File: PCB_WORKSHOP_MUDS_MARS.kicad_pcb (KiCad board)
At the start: 2 copper layers, 44.7 x 72.4 mm, 48 parts, among them J1 Conn_01x02_Pin, J2 Conn_01x02_Pin, J3 Conn_01x15_Socket, J4 Conn_01x15_Socket, J5 Conn_01x15_Socket, J6 Conn_01x02_Pin, M1 SI2300, SW1 SW_Push, U1 L9110S

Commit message: Silk screen adjustments
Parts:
- added G***: LOGO, LOGO, F.Cu at (168.1, 124.5)
- moved G*** 6.60 mm to (177.3, 124.7)
- renumbered J2 to J1, J6 to J2, J1 to J3, J3 to J4, J4 to J5, J5 to J6, M1 to U2
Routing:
- net KITC_GND: track 105.5 -> 134.0 mm
- net M_VCC: track 74.6 -> 70.0 mm
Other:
- board text added: "&"
- board text added: "A"
- board text added: "B"
- board text added: "BTN"
- board text added: "GND"
- board text added: "L1"
- board text added: "L10"
- board text added: "L11"
- board text added: "L2"
- board text added: "L3"
- board text added: "L4"
- board text added: "L5"
- board text added: "L6"
- board text added: "L7"
- board text added: "L8"
- board text added: "L9"
- board text added: "M1"
- board text added: "M1A"
- board text added: "M1B"
- board text added: "M2"

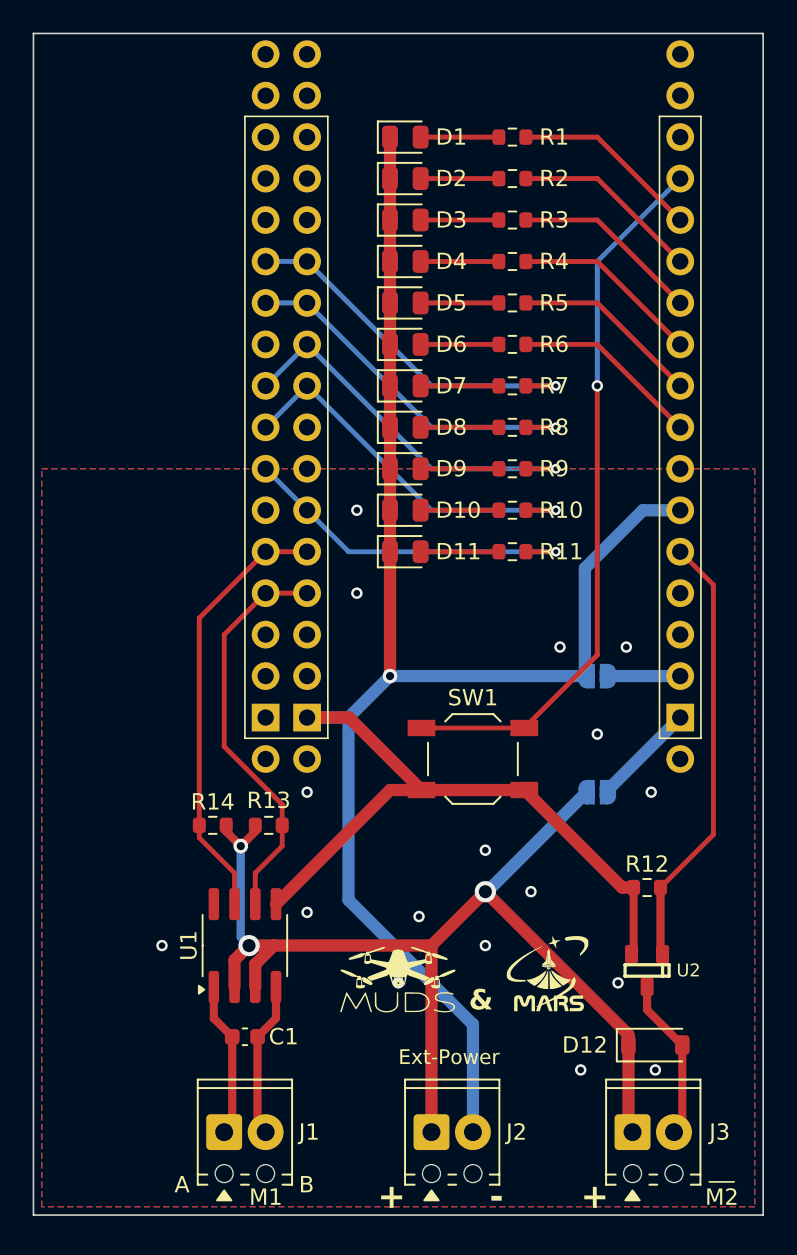
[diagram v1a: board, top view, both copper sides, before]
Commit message: added README, fixed examples
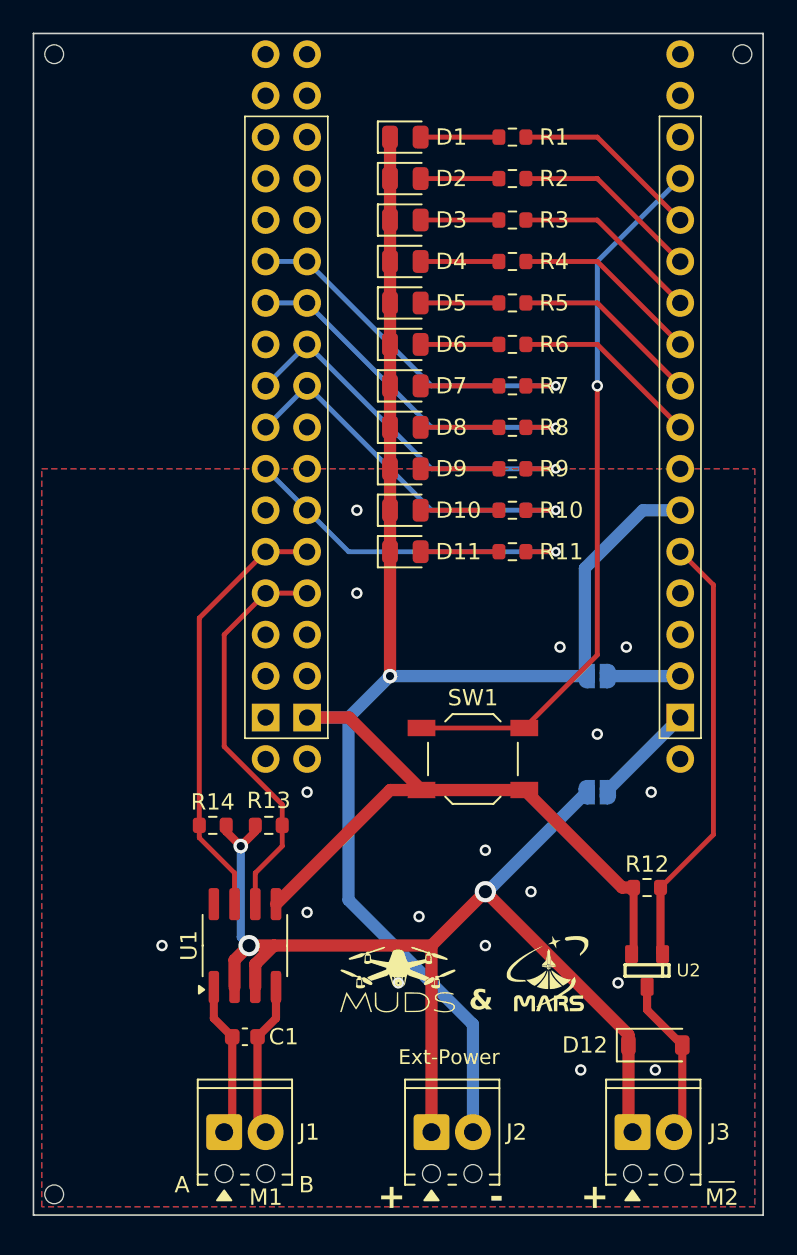
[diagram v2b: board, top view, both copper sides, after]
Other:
- outline, holes or cut-outs redrawn
- board text added: "JLCJLCJLCJLC"
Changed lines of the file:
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@@
+		(layer "Edge.Cuts")
+	)
+	(gr_circle
+		(center 189.23 68.58)
+		(end 189.806 68.58)
+		(stroke
+			(width 0.05)
+			(type solid)
+		)
+		(fill no)
+		(layer "Edge.Cuts")
+	)
+	(gr_circle
+		(center 147.066 68.58)
+		(end 147.642 68.58)
+		(stroke
+			(width 0.05)
+			(type solid)
+		)
+		(fill no)
+		(layer "Edge.Cuts")
+	)
+	(gr_circle
+		(center 147.066 138.43)
+		(end 147.642 138.43)
+		(stroke
+			(width 0.05)
+			(type solid)
+		)
+		(fill no)
 		(layer "Edge.Cuts")
 	)
@@
 		)
 	)
+	(gr_text "JLCJLCJLCJLC"
+		(at 173.736 102.87 90)
+		(layer "B.SilkS")
+		(effects
+			(font
+				(size 1 1)
+				(thickness 0.1)
+			)
+			(justify left bottom mirror)
+		)
+	)

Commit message: Forgot silkscreen blocks
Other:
- board text added: "BOPPIT Game"
- board text added: "H-Bridge Driver"
- board text added: "UniDir Motor Driver"
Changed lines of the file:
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@@
 		(tags "resistor")
 		(property "Reference" "R14"
-			(at 0 -1.43 0)
+			(at 0 1.524 0)
 			(layer "F.SilkS")
 			(effects
@@
 		(tags "capacitor")
 		(property "Reference" "C1"
-			(at 2.375 0 0)
+			(at -2.54 0 0)
 			(layer "F.SilkS")
 			(effects
@@
 		(tags "resistor")
 		(property "Reference" "R13"
-			(at 0 1.524 0)
+			(at 0 -1.524 0)
 			(layer "F.SilkS")
 			(effects
@@
 		(tags "resistor")
 		(property "Reference" "R12"
-			(at 0 -1.43 0)
+			(at 0 1.524 0)
 			(layer "F.SilkS")
 			(effects
@@
 		(tags "SOD-123")
 		(property "Reference" "D12"
-			(at -4.318 0 0)
+			(at -0.254 -2.032 0)
 			(layer "F.SilkS")
 			(effects
@@
 		(layer "F.SilkS")
 	)
+	(gr_line
+		(start 162.052 131.064)
+		(end 163.83 129.286)
+		(stroke
+			(width 0.1)
+			(type default)
+		)
+		(layer "F.SilkS")
+	)
+	(gr_line
+		(start 162.052 114.554)
+		(end 155.702 114.554)
+		(stroke
+			(width 0.1)
+			(type default)
+		)
+		(layer "F.SilkS")
+	)
+	(gr_line
+		(start 155.702 114.554)
+		(end 154.178 116.078)
+		(stroke
+			(width 0.1)
+			(type default)
+		)
+		(layer "F.SilkS")
+	)
 	(gr_rect
 		(start 158.75 72.39)
@@
 	)
 	(gr_line
+		(start 162.052 114.554)
+		(end 163.83 116.332)
+		(stroke
+			(width 0.1)
+			(type default)
+		)
+		(layer "F.SilkS")
+	)
+	(gr_line
+		(start 180.848 118.618)
+		(end 181.61 117.856)
+		(stroke
+			(width 0.1)
+			(type default)
+		)
+		(layer "F.SilkS")
+	)
+	(gr_line
+		(start 154.178 129.794)
+		(end 154.178 116.078)
+		(stroke
+			(width 0.1)
+			(type default)
+		)
+		(layer "F.SilkS")
+	)
+	(gr_line
 		(start 187.198 137.668)
 		(end 188.722 137.668)
@@
 	)
 	(gr_line
+		(start 180.848 129.286)
+		(end 180.848 118.618)
+		(stroke
+			(width 0.1)
+			(type default)
+		)
+		(layer "F.SilkS")
+	)
+	(gr_line
+		(start 163.83 129.286)
+		(end 163.83 116.332)
+		(stroke
+			(width 0.1)
+			(type default)
+		)
+		(layer "F.SilkS")
+	)
+	(gr_line
+		(start 181.61 117.856)
+		(end 189.23 117.856)
+		(stroke
+			(width 0.1)
+			(type default)
+		)
+		(layer "F.SilkS")
+	)
+	(gr_rect
+		(start 165.862 71.628)
+		(end 180.848 115.316)
+		(stroke
+			(width 0.1)
+			(type default)
+		)
+		(fill no)
+		(layer "F.SilkS")
+	)
+	(gr_line
+		(start 155.448 131.064)
+		(end 154.178 129.794)
+		(stroke
+			(width 0.1)
+			(type default)
+		)
+		(layer "F.SilkS")
+	)
+	(gr_line
 		(start 164.338 89.408)
 		(end 163.83 88.9)
@@
 		)
 	)
+	(gr_text "UniDir Motor Driver"
+		(at 188.976 131.572 90)
+		(layer "F.SilkS")
+		(effects
+			(font
+				(size 0.9 0.9)
+				(thickness 0.15)
+			)
+			(justify left bottom)
+		)
+	)
 	(gr_text "Ext-Power"
 		(at 168.148 130.556 0)
@@
 		)
 	)
+	(gr_text "BOPPIT Game"
+		(at 179.832 114.554 90)
+		(layer "F.SilkS")
+		(effects
+			(font
+				(size 1 1)
+				(thickness 0.1)
+			)
+			(justify left bottom)
+		)
+	)
 	(gr_text "A"
 		(at 154.432 138.43 0)
@@
 				(bold yes)
 			)
+			(justify left bottom)
+		)
+	)
+	(gr_text "H-Bridge Driver"
+		(at 163.322 127.762 90)
+		(layer "F.SilkS")
+		(effects
+			(font
+				(size 0.9 0.9)
+				(thickness 0.15)
+				(bold yes)
+			)

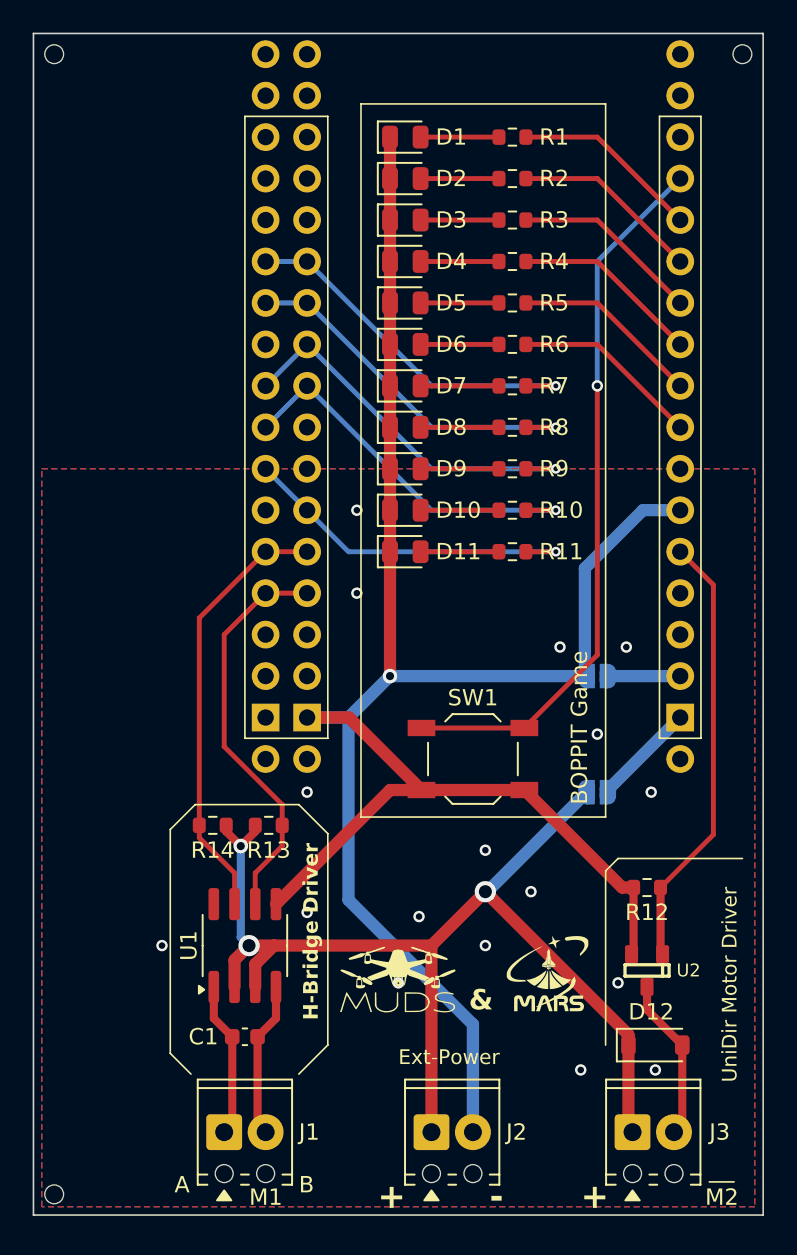
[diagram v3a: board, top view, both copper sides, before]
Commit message: Custom silkscreen images for order
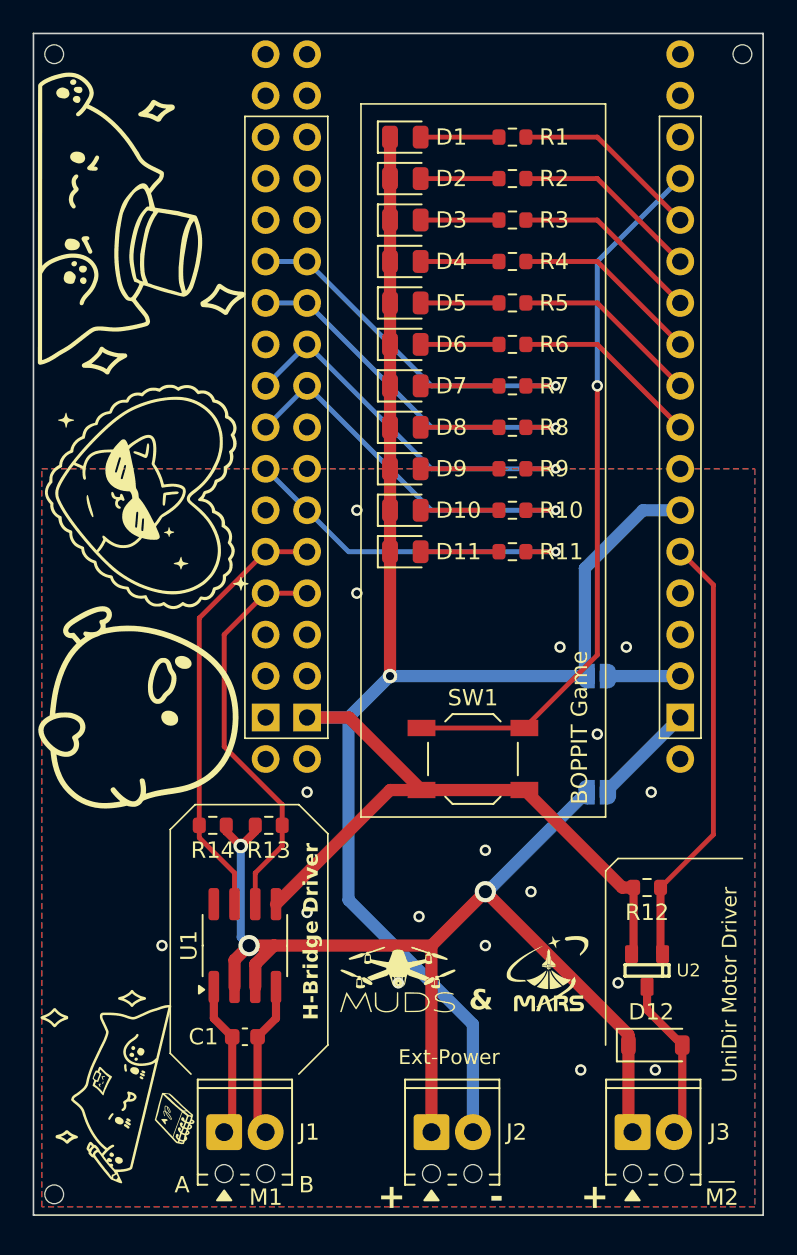
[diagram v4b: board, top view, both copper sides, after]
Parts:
- added G***: LOGO, LOGO, F.Cu at (152.1, 108.7)
- added G***: LOGO, LOGO, F.Cu at (150.9, 131.8)
- added G***: LOGO, LOGO, F.Cu at (152.7, 95.8)
- added G***: LOGO, LOGO, F.Cu at (149.6, 78.2)
- added G***: LOGO, LOGO, B.Cu at (177.5, 123.7)
- added G***: LOGO, LOGO, B.Cu at (158.8, 121.9)
